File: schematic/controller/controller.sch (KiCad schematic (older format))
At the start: 0 parts

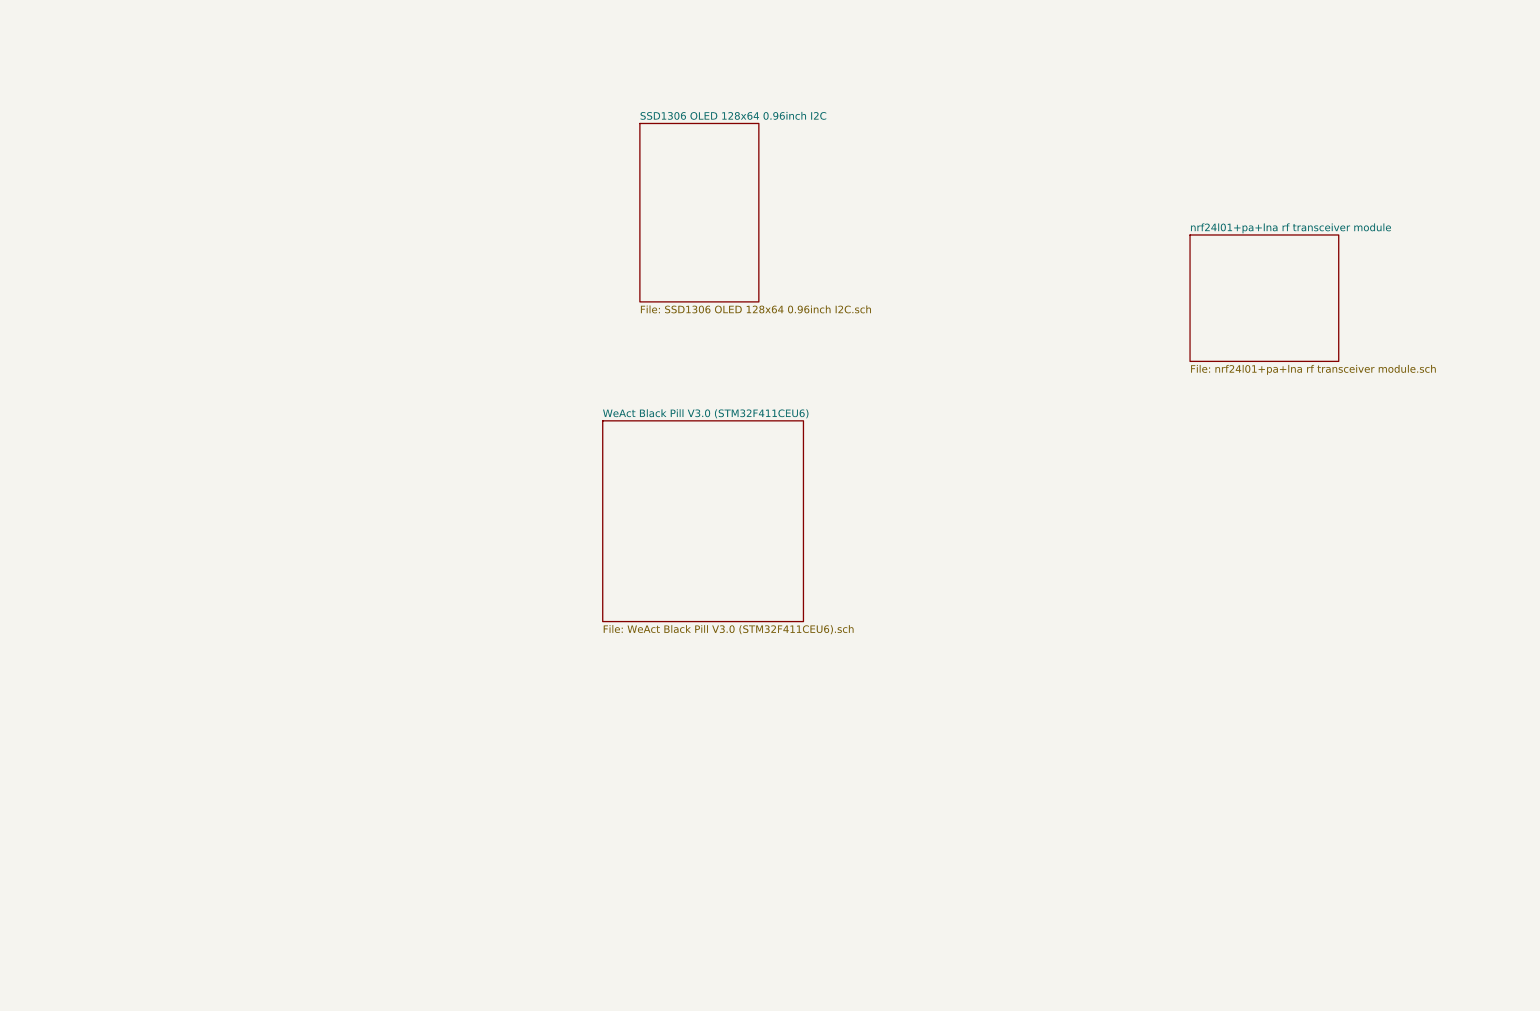
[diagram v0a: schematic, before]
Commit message: Add controller schematic
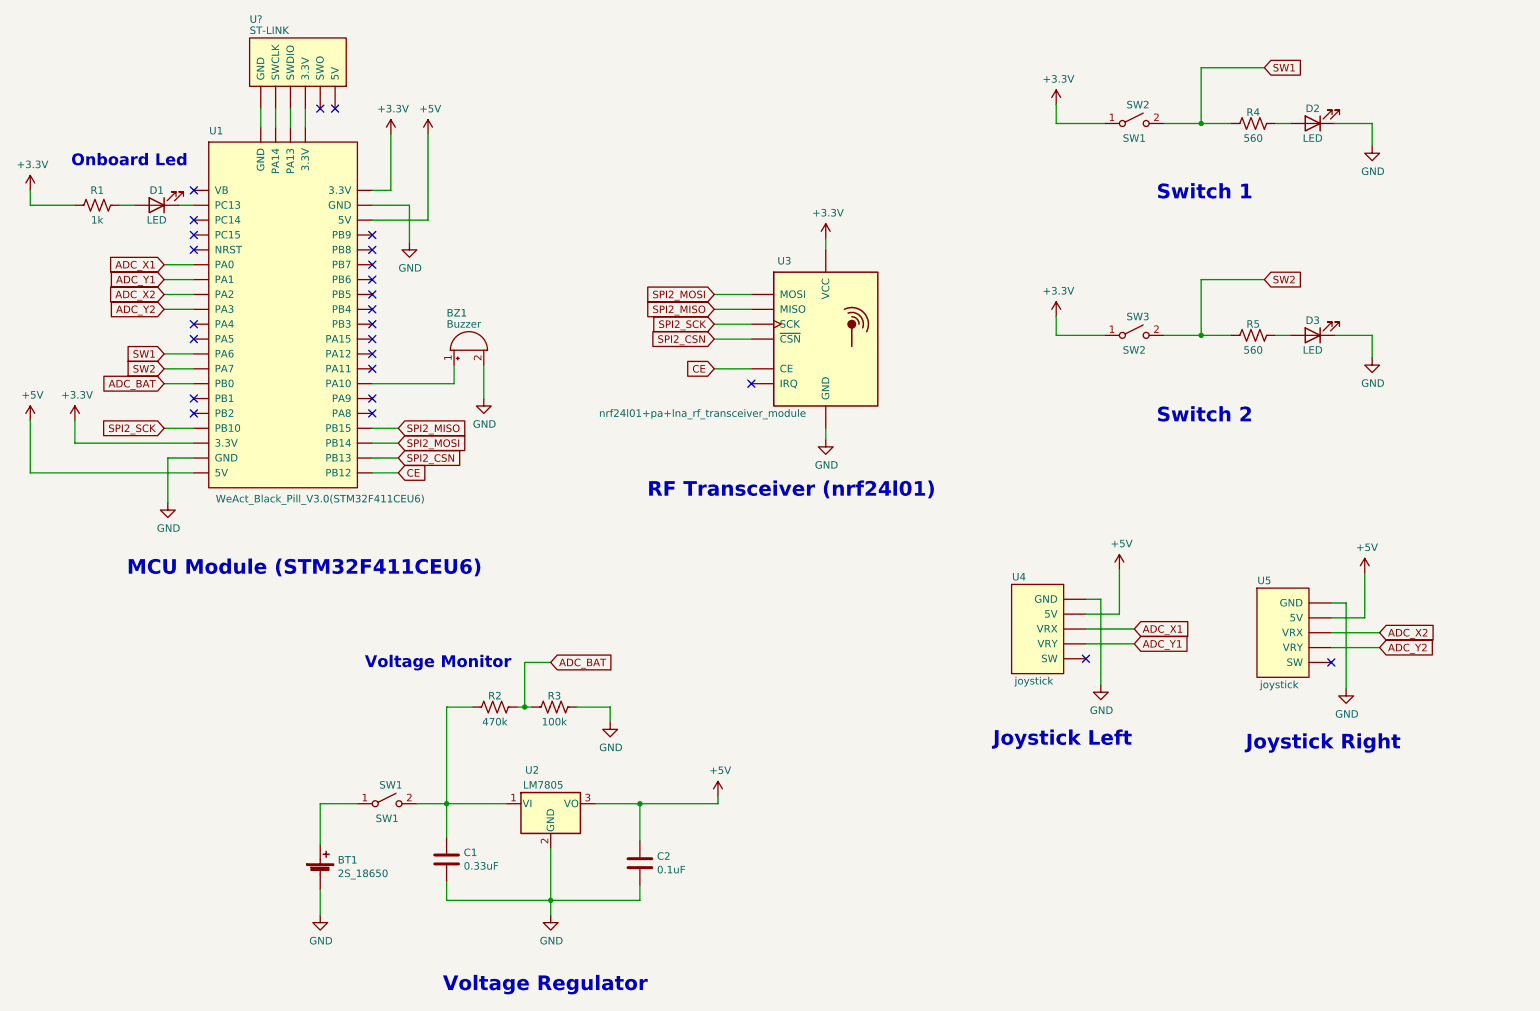
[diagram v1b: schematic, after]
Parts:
- added BT1: 2S_18650, symbol Device:Battery_Cell
- added BZ1: Buzzer, symbol Device:Buzzer
- added C1: 0.33uF, symbol Device:C
- added C2: 0.1uF, symbol Device:C
- added D1, D2, D3: LED, symbol Device:LED
- added R1: 1k, symbol Device:R_US
- added R2: 470k, symbol Device:R_US
- added R3: 100k, symbol Device:R_US
- added R4, R5: 560, symbol Device:R_US
- added SW1, SW2: SW1, symbol Switch:SW_SPST
- added SW3: SW2, symbol Switch:SW_SPST
- added U1: WeAct_Black_Pill_V3.0(STM32F411CEU6), symbol controller_symbol:WeAct_Black_Pill_V3.0(STM32F411CEU6)
- added U2: LM7805, Package_TO_SOT_THT:TO-220-3_Vertical, symbol Regulator_Linear:LM7805_TO220
- added U3: nrf24l01+pa+lna_rf_transceiver_module, symbol controller_symbol:nrf24l01+pa+lna_rf_transceiver_module
- added U4, U5: joystick, symbol controller_symbol:joystick
- added U?: ST-LINK, symbol controller_symbol:ST-LINK
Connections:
- new net: D1.1 (K), U1.~ (VB)
- new net: BZ1.1 (-), U1.~ (VB)
- new net: U1.~ (VB), U?.~ (SWO) (x4)
- new net: D1.2 (A), R1.1
- new net: D2.2 (A), R4.1
- new net: D3.2 (A), R5.1
- new net: C1.1, R2.2, SW1.2 (B), U2.1 (VI)
- new net: BT1.1 (+), SW1.1 (A)
- new net +3V3: R1.2, SW2.1 (A), SW3.1 (A), U1.~ (VB), U3.~ (~CSN)
- new net +5V: C2.1, U1.~ (VB), U2.3 (VO), U4.~ (VRY), U5.~ (VRY)
- new net ADC_BAT: R2.1, R3.2, U1.~ (VB)
- new net ADC_X1: U1.~ (VB), U4.~ (VRY)
- new net ADC_X2: U1.~ (VB), U5.~ (VRY)
- new net ADC_Y1: U1.~ (VB), U4.~ (VRY)
- new net ADC_Y2: U1.~ (VB), U5.~ (VRY)
- new net CE: U1.~ (VB), U3.~ (~CSN)
- new net GND: BT1.2 (-), BZ1.2 (+), C1.2, C2.2, D2.1 (K), D3.1 (K), R3.1, U1.~ (VB), U2.2 (GND), U3.~ (~CSN), U4.~ (VRY), U5.~ (VRY)
- new net SPI2_CSN: U1.~ (VB), U3.~ (~CSN)
- new net SPI2_MISO: U1.~ (VB), U3.~ (~CSN)
- new net SPI2_MOSI: U1.~ (VB), U3.~ (~CSN)
- new net SPI2_SCK: U1.~ (VB), U3.~ (~CSN)
- new net SW1: R4.2, SW2.2 (B), U1.~ (VB)
- new net SW2: R5.2, SW3.2 (B), U1.~ (VB)
- no-connect marks 0 -> 25
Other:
- note added: "Joystick Left"
- note added: "Joystick Right"
- note added: "MCU Module (STM32F411CEU6)"
- note added: "Onboard Led"
- note added: "RF Transceiver (nrf24l01)"
- note added: "Switch 1"
- note added: "Switch 2"
- note added: "Voltage Monitor"
- note added: "Voltage Regulator"
